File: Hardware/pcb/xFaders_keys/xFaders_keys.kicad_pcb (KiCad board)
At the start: 2 copper layers, 354.3 x 53.3 mm, 88 parts, among them J1 Conn_02x10_Odd_Even, SW1 SW_Push, SW10 SW_Push, SW11 SW_Push, SW12 SW_Push, SW13 SW_Push, SW14 SW_Push, SW15 SW_Push, SW16 SW_Push, SW17 SW_Push, SW18 SW_Push, SW19 SW_Push, SW2 SW_Push, SW20 SW_Push, SW21 SW_Push, SW22 SW_Push, SW23 SW_Push, SW24 SW_Push, SW25 SW_Push, SW26 SW_Push, SW27 SW_Push, SW28 SW_Push, SW29 SW_Push, SW3 SW_Push, SW30 SW_Push, SW31 SW_Push, SW32 SW_Push, SW33 SW_Push, SW34 SW_Push, SW35 SW_Push, SW36 SW_Push, SW37 SW_Push, SW38 SW_Push, SW39 SW_Push, SW4 SW_Push, SW40 SW_Push, SW41 SW_Push, SW42 SW_Push, SW43 SW_Push, SW44 SW_Push, SW45 SW_Push, SW5 SW_Push, SW6 SW_Push, SW7 SW_Push, SW8 SW_Push, SW9 SW_Push

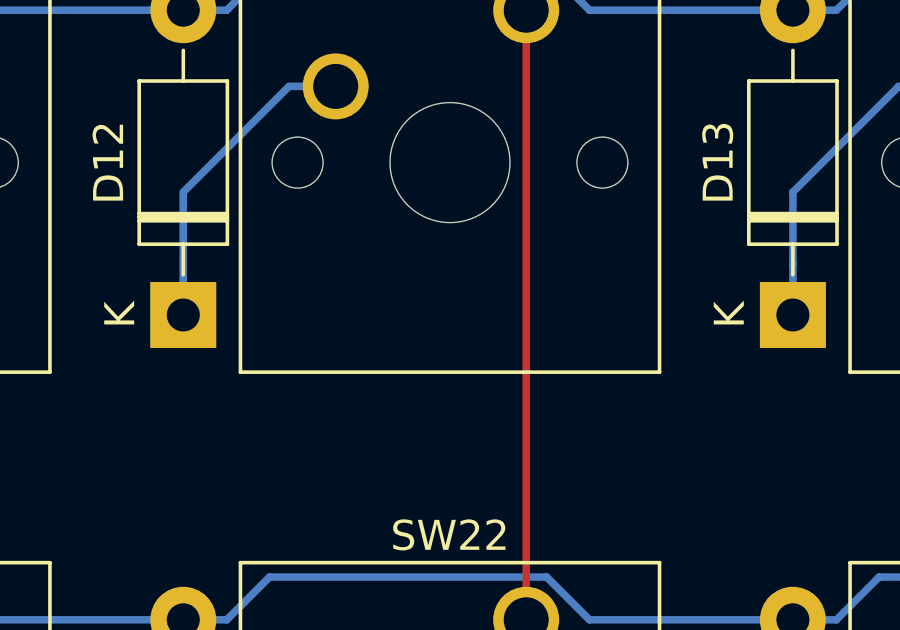
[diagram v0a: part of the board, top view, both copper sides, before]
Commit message: Add kicad library for SK6812 MINI-E RGB LEDs
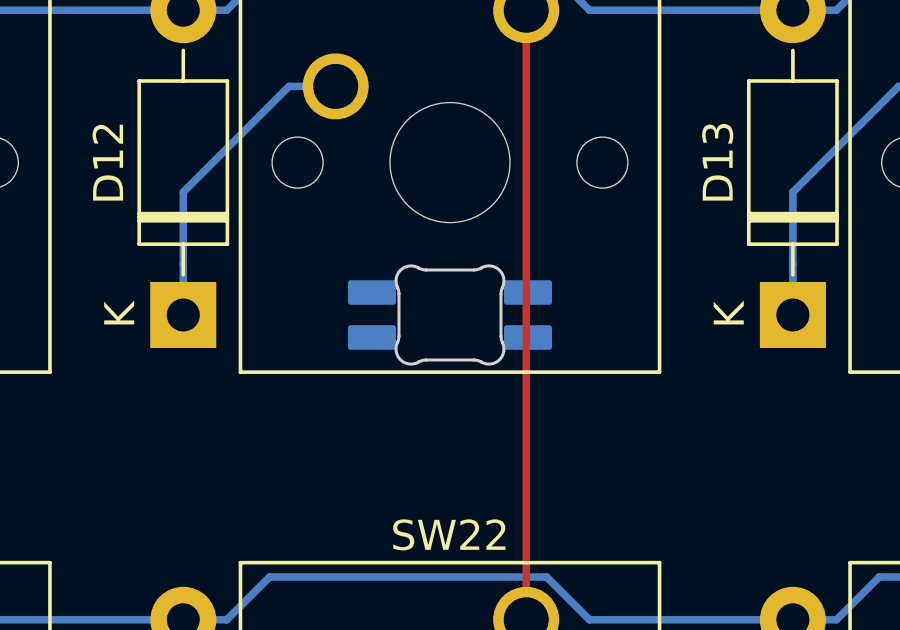
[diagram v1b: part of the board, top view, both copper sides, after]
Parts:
- added D31: SK6812MINI-E, kicad-keyboard-parts:MX_SK6812MINI-E, F.Cu at (188.0, 149.9)

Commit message: Rotate keys in bottom row to make room for leds
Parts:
- J1: moved to B.Cu
- moved J1 21.0 mm to (383.5, 178.4)
- moved D31 20.3 mm to (188.0, 170.2)
- moved SW45 11.4 mm to (358.1, 185.4), turned to 180 degrees
- moved SW26 11.4 mm to (165.1, 185.4), turned to 180 degrees
- moved SW27 11.4 mm to (185.4, 185.4), turned to 180 degrees
- moved SW30 11.4 mm to (246.4, 185.4), turned to 180 degrees
- moved SW11 11.4 mm to (53.3, 185.4), turned to 180 degrees
- moved SW12 11.4 mm to (73.7, 185.4), turned to 180 degrees
- moved SW13 11.4 mm to (94.0, 185.4), turned to 180 degrees
- moved SW14 11.4 mm to (114.3, 185.4), turned to 180 degrees
- moved SW15 11.4 mm to (134.6, 185.4), turned to 180 degrees
- moved SW28 11.4 mm to (205.7, 185.4), turned to 180 degrees
- moved SW29 11.4 mm to (226.1, 185.4), turned to 180 degrees
- moved SW36 11.4 mm to (276.9, 185.4), turned to 180 degrees
- moved SW42 11.4 mm to (297.2, 185.4), turned to 180 degrees
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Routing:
- net Col0: track 364.8 -> 20.3 mm
- net Col1: track 345.6 -> 20.3 mm
- net Col2: track 327.1 -> 20.3 mm
- net Col4: track 315.7 -> 20.3 mm, vias 1 -> 0
- net Col3: track 308.6 -> 20.3 mm
- net Col5: track 275.9 -> 20.3 mm, vias 1 -> 0
- net Col6: track 243.6 -> 20.3 mm, vias 2 -> 0
- net Col7: track 219.7 -> 20.3 mm, vias 1 -> 0
- net Col9: track 200.7 -> 20.3 mm
- net Col8: track 195.8 -> 20.3 mm, vias 1 -> 0
- net Col10: track 168.8 -> 20.3 mm
- net Col11: track 145.1 -> 20.3 mm
- net Col12: track 118.6 -> 20.3 mm
- net Col13: track 100.6 -> 20.3 mm
- net Row0: track 370.7 -> 321.3 mm
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
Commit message: Add RGB LEDs and capacitors to Schema and PCB
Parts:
- removed D31: SK6812MINI-E, kicad-keyboard-parts:MX_SK6812MINI-E
- added C1: 100nF, Capacitor_SMD:C_0603_1608Metric_Pad1.05x0.95mm_HandSolder, B.Cu at (50.8, 153.9)
- added C10: 100nF, Capacitor_SMD:C_0603_1608Metric_Pad1.05x0.95mm_HandSolder, B.Cu at (243.8, 153.9)
- added C11: 100nF, Capacitor_SMD:C_0603_1608Metric_Pad1.05x0.95mm_HandSolder, B.Cu at (274.3, 153.9)
- added C12: 100nF, Capacitor_SMD:C_0603_1608Metric_Pad1.05x0.95mm_HandSolder, B.Cu at (294.6, 153.9)
- added C13: 100nF, Capacitor_SMD:C_0603_1608Metric_Pad1.05x0.95mm_HandSolder, B.Cu at (315.0, 153.9)
- added C14: 100nF, Capacitor_SMD:C_0603_1608Metric_Pad1.05x0.95mm_HandSolder, B.Cu at (335.3, 153.9)
- added C15: 100nF, Capacitor_SMD:C_0603_1608Metric_Pad1.05x0.95mm_HandSolder, B.Cu at (355.6, 153.9)
- added C16: 100nF, Capacitor_SMD:C_0603_1608Metric_Pad1.05x0.95mm_HandSolder, B.Cu at (50.8, 173.6)
- added C17: 100nF, Capacitor_SMD:C_0603_1608Metric_Pad1.05x0.95mm_HandSolder, B.Cu at (71.1, 173.6)
- added C18: 100nF, Capacitor_SMD:C_0603_1608Metric_Pad1.05x0.95mm_HandSolder, B.Cu at (91.4, 173.4)
- added C19: 100nF, Capacitor_SMD:C_0603_1608Metric_Pad1.05x0.95mm_HandSolder, B.Cu at (111.8, 173.4)
- added C2: 100nF, Capacitor_SMD:C_0603_1608Metric_Pad1.05x0.95mm_HandSolder, B.Cu at (71.1, 153.9)
- added C20: 100nF, Capacitor_SMD:C_0603_1608Metric_Pad1.05x0.95mm_HandSolder, B.Cu at (132.1, 173.4)
- added C21: 100nF, Capacitor_SMD:C_0603_1608Metric_Pad1.05x0.95mm_HandSolder, B.Cu at (162.6, 173.4)
- added C22: 100nF, Capacitor_SMD:C_0603_1608Metric_Pad1.05x0.95mm_HandSolder, B.Cu at (182.9, 173.6)
- added C23: 100nF, Capacitor_SMD:C_0603_1608Metric_Pad1.05x0.95mm_HandSolder, B.Cu at (203.2, 173.4)
- added C24: 100nF, Capacitor_SMD:C_0603_1608Metric_Pad1.05x0.95mm_HandSolder, B.Cu at (223.5, 173.6)
- added C25: 100nF, Capacitor_SMD:C_0603_1608Metric_Pad1.05x0.95mm_HandSolder, B.Cu at (243.8, 173.6)
- added C26: 100nF, Capacitor_SMD:C_0603_1608Metric_Pad1.05x0.95mm_HandSolder, B.Cu at (274.3, 173.6)
- added C27: 100nF, Capacitor_SMD:C_0603_1608Metric_Pad1.05x0.95mm_HandSolder, B.Cu at (294.6, 173.6)
- added C28: 100nF, Capacitor_SMD:C_0603_1608Metric_Pad1.05x0.95mm_HandSolder, B.Cu at (315.0, 173.6)
- added C29: 100nF, Capacitor_SMD:C_0603_1608Metric_Pad1.05x0.95mm_HandSolder, B.Cu at (335.3, 173.6)
- added C3: 100nF, Capacitor_SMD:C_0603_1608Metric_Pad1.05x0.95mm_HandSolder, B.Cu at (91.4, 153.9)
- added C30: 100nF, Capacitor_SMD:C_0603_1608Metric_Pad1.05x0.95mm_HandSolder, B.Cu at (355.6, 173.6)
- added C4: 100nF, Capacitor_SMD:C_0603_1608Metric_Pad1.05x0.95mm_HandSolder, B.Cu at (111.8, 153.7)
- added C5: 100nF, Capacitor_SMD:C_0603_1608Metric_Pad1.05x0.95mm_HandSolder, B.Cu at (132.1, 153.9)
- added C6: 100nF, Capacitor_SMD:C_0603_1608Metric_Pad1.05x0.95mm_HandSolder, B.Cu at (162.6, 153.7)
- added C7: 100nF, Capacitor_SMD:C_0603_1608Metric_Pad1.05x0.95mm_HandSolder, B.Cu at (182.9, 153.7)
- added C8: 100nF, Capacitor_SMD:C_0603_1608Metric_Pad1.05x0.95mm_HandSolder, B.Cu at (203.2, 153.7)
- added C9: 100nF, Capacitor_SMD:C_0603_1608Metric_Pad1.05x0.95mm_HandSolder, B.Cu at (223.5, 153.7)
- added J2: Conn_01x02_Female, Connector_PinHeader_2.54mm:PinHeader_1x02_P2.54mm_Vertical, F.Cu at (383.5, 142.2)
- added R1: 500, Resistor_THT:R_Axial_DIN0204_L3.6mm_D1.6mm_P5.08mm_Horizontal, F.Cu at (370.2, 172.7)
- added R2: 500, Resistor_THT:R_Axial_DIN0204_L3.6mm_D1.6mm_P5.08mm_Horizontal, F.Cu at (61.0, 160.0)
- added RGB1: SK6812MINI-E, kicad-keyboard-parts:MX_SK6812MINI-E, F.Cu at (55.9, 149.9)
- added RGB10: SK6812MINI-E, kicad-keyboard-parts:MX_SK6812MINI-E, F.Cu at (248.9, 149.9)
- added RGB11: SK6812MINI-E, kicad-keyboard-parts:MX_SK6812MINI-E, F.Cu at (279.4, 149.9)
- added RGB12: SK6812MINI-E, kicad-keyboard-parts:MX_SK6812MINI-E, F.Cu at (299.7, 149.9)
- added RGB13: SK6812MINI-E, kicad-keyboard-parts:MX_SK6812MINI-E, F.Cu at (320.0, 149.9)
- added RGB14: SK6812MINI-E, kicad-keyboard-parts:MX_SK6812MINI-E, F.Cu at (340.4, 149.9)
- added RGB15: SK6812MINI-E, kicad-keyboard-parts:MX_SK6812MINI-E, F.Cu at (360.7, 149.9)
- added RGB16: SK6812MINI-E, kicad-keyboard-parts:MX_SK6812MINI-E, F.Cu at (55.9, 170.2)
- added RGB17: SK6812MINI-E, kicad-keyboard-parts:MX_SK6812MINI-E, F.Cu at (76.2, 170.2)
- added RGB18: SK6812MINI-E, kicad-keyboard-parts:MX_SK6812MINI-E, F.Cu at (96.5, 170.2)
- added RGB19: SK6812MINI-E, kicad-keyboard-parts:MX_SK6812MINI-E, F.Cu at (116.8, 170.2)
- added RGB2: SK6812MINI-E, kicad-keyboard-parts:MX_SK6812MINI-E, F.Cu at (76.2, 149.9)
- added RGB20: SK6812MINI-E, kicad-keyboard-parts:MX_SK6812MINI-E, F.Cu at (137.2, 170.2)
- added RGB21: SK6812MINI-E, kicad-keyboard-parts:MX_SK6812MINI-E, F.Cu at (167.6, 170.2)
- added RGB22: SK6812MINI-E, kicad-keyboard-parts:MX_SK6812MINI-E, F.Cu at (188.0, 170.2)
- added RGB23: SK6812MINI-E, kicad-keyboard-parts:MX_SK6812MINI-E, F.Cu at (208.3, 170.2)
- added RGB24: SK6812MINI-E, kicad-keyboard-parts:MX_SK6812MINI-E, F.Cu at (228.6, 170.2)
- added RGB25: SK6812MINI-E, kicad-keyboard-parts:MX_SK6812MINI-E, F.Cu at (248.9, 170.2)
- added RGB26: SK6812MINI-E, kicad-keyboard-parts:MX_SK6812MINI-E, F.Cu at (279.4, 170.2)
- added RGB27: SK6812MINI-E, kicad-keyboard-parts:MX_SK6812MINI-E, F.Cu at (299.7, 170.2)
- added RGB28: SK6812MINI-E, kicad-keyboard-parts:MX_SK6812MINI-E, F.Cu at (320.0, 170.2)
- added RGB29: SK6812MINI-E, kicad-keyboard-parts:MX_SK6812MINI-E, F.Cu at (340.4, 170.2)
- added RGB3: SK6812MINI-E, kicad-keyboard-parts:MX_SK6812MINI-E, F.Cu at (96.5, 149.9)
- added RGB30: SK6812MINI-E, kicad-keyboard-parts:MX_SK6812MINI-E, F.Cu at (360.7, 170.2)
- added RGB4: SK6812MINI-E, kicad-keyboard-parts:MX_SK6812MINI-E, F.Cu at (116.8, 149.9)
- added RGB5: SK6812MINI-E, kicad-keyboard-parts:MX_SK6812MINI-E, F.Cu at (137.2, 149.9)
- added RGB6: SK6812MINI-E, kicad-keyboard-parts:MX_SK6812MINI-E, F.Cu at (167.6, 149.9)
- added RGB7: SK6812MINI-E, kicad-keyboard-parts:MX_SK6812MINI-E, F.Cu at (188.0, 149.9)
- added RGB8: SK6812MINI-E, kicad-keyboard-parts:MX_SK6812MINI-E, F.Cu at (208.3, 149.9)
- added RGB9: SK6812MINI-E, kicad-keyboard-parts:MX_SK6812MINI-E, F.Cu at (228.6, 149.9)
- D1, D10, D11, D12, D13, D14, D15, D16, D17, D18, D19, D2, D20, D21, D22, D23, D24, D25, D26, D27, D28, D29, D3, D30, D4, D5, D6, D7, D8, D9: footprint Diode_THT:D_DO-41_SOD81_P10.16mm_Horizontal -> Diode_THT:D_DO-35_SOD27_P10.16mm_Horizontal
- moved D5 0.63 mm to (128.9, 154.9)
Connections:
- J1 pad 1: VCC3V3 -> DataIn
- J1 pad 18: Net-(J1-Pad18) -> DataOut
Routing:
- net +5V: track 0.00 -> 936.9 mm, vias 0 -> 8
- net Col0: track 20.3 -> 386.8 mm, vias 0 -> 2
- net Col1: track 20.3 -> 368.8 mm, vias 0 -> 2
- net Net-(RGB15-Pad4): track 0.00 -> 337.9 mm, vias 0 -> 4
- net Col2: track 20.3 -> 347.6 mm, vias 0 -> 2
- net DataOut: track 0.00 -> 325.9 mm
- net Col3: track 20.3 -> 328.0 mm, vias 0 -> 2
- net Col4: track 20.3 -> 289.3 mm, vias 0 -> 2
- net Col5: track 20.3 -> 258.4 mm, vias 0 -> 2
- net Col6: track 20.3 -> 252.6 mm, vias 0 -> 2
- net Col7: track 20.3 -> 229.6 mm
- net Col8: track 20.3 -> 205.0 mm
- net Col9: track 20.3 -> 199.8 mm, vias 0 -> 2
- net Col10: track 20.3 -> 171.4 mm, vias 0 -> 2
- net Col11: track 20.3 -> 153.1 mm, vias 0 -> 2
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- added copper zone on B.Cu, net GND
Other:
- net class RGB_5V added: clearance 0.2, trace_width 0.75, via_dia 0.8, via_drill 0.4
- board text added: "+5V"
- board text added: "GND"

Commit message: Update PCB for new RGB LEDs and 5V power supply
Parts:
- added J3: Conn_01x02_Female, Connector_PinHeader_2.54mm:PinHeader_1x02_P2.54mm_Vertical, B.Cu at (121.9, 141.0)
- J2: moved to B.Cu
- moved J2 2.54 mm to (386.1, 142.2)
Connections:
- J2 pad 1: +5V -> GND
- J2 pad 2: GND -> +5V
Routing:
- net +5V: track 936.9 -> 938.2 mm
